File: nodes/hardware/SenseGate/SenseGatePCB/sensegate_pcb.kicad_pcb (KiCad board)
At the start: 2 copper layers, 64.6 x 110 mm, 32 parts, among them J3 Conn_01x02_Socket, J4 Conn_01x24_Pin, J5 Conn_01x04_Socket, J6 Conn_01x04_Socket, J7 Conn_01x04_Socket, J8 Conn_01x04_Socket, J9 Conn_01x04_Socket, Q4 SS8050, SW5 SW_DPDT_x2, U1 DD05CVSA, U2 mt3608_dcdc_converter

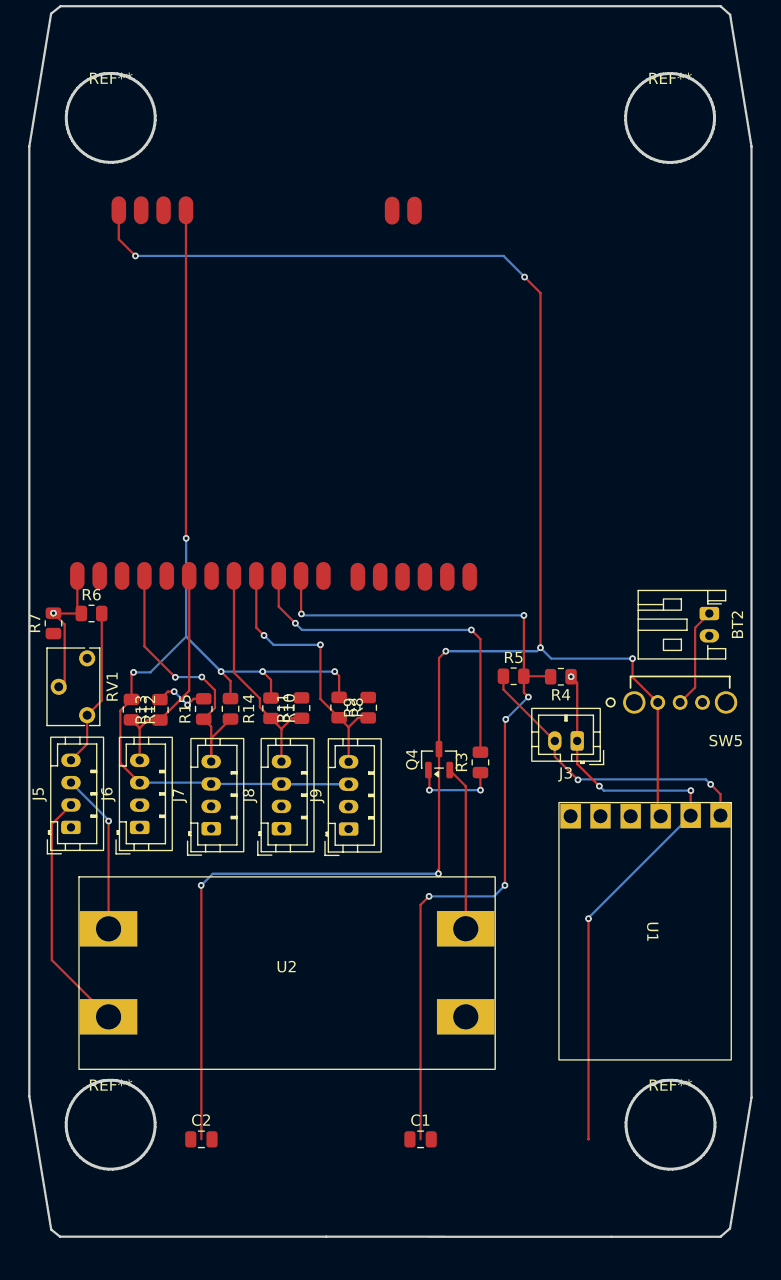
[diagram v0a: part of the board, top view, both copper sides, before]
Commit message: mounting holes for battery added and add schematic for 7.8mm holes
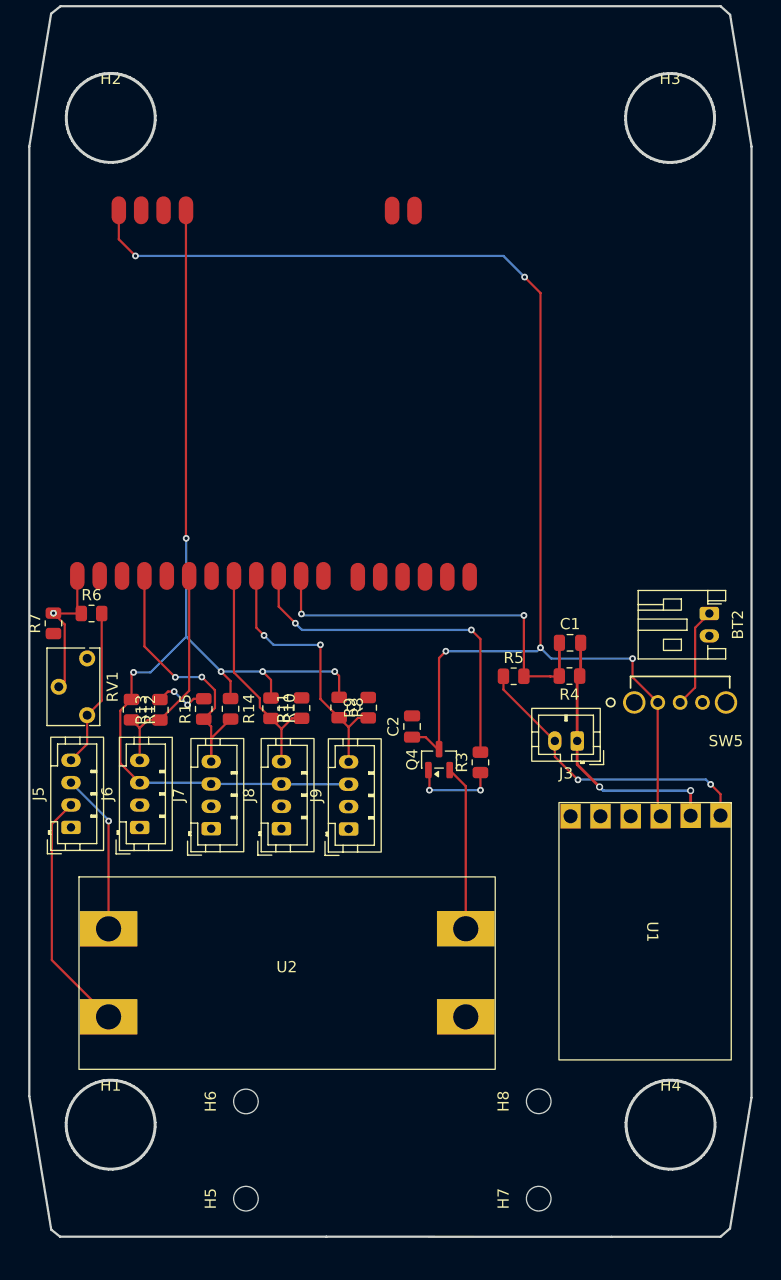
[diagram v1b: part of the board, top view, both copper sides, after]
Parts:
- removed REF** (x4): mounting_hole_7.8mm, SenseGateLib:mounting_hole_7.8mm
- added H1: MountingHole, SenseGateLib:mounting_hole_7.8mm, F.Cu at (102.6, 139.0)
- added H2: MountingHole, SenseGateLib:mounting_hole_7.8mm, F.Cu at (102.6, 49.0)
- added H3: MountingHole, SenseGateLib:mounting_hole_7.8mm, F.Cu at (152.6, 49.0)
- added H4: MountingHole, SenseGateLib:mounting_hole_7.8mm, F.Cu at (152.6, 139.0)
- added H5: MountingHole, MountingHole:MountingHole_2.2mm_M2, F.Cu at (114.7, 145.6)
- added H6: MountingHole, MountingHole:MountingHole_2.2mm_M2, F.Cu at (114.7, 136.9)
- added H7: MountingHole, MountingHole:MountingHole_2.2mm_M2, F.Cu at (140.8, 145.6)
- added H8: MountingHole, MountingHole:MountingHole_2.2mm_M2, F.Cu at (140.8, 136.9)
- moved C1 46.3 mm to (143.7, 95.9)
- moved C2 41.4 mm to (129.5, 103.4), turned to 90 degrees
- moved R4 0.77 mm to (143.6, 98.9)
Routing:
- net VBAT: track 170.8 -> 118.2 mm, vias 7 -> 5
- net MON_SOLAR: track 80.2 -> 35.0 mm, vias 6 -> 2
- net Net-(J3-Pin_1): track 54.1 -> 24.4 mm, vias 4 -> 2
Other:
- board text added: "SenseGate v1 16/06/2026"

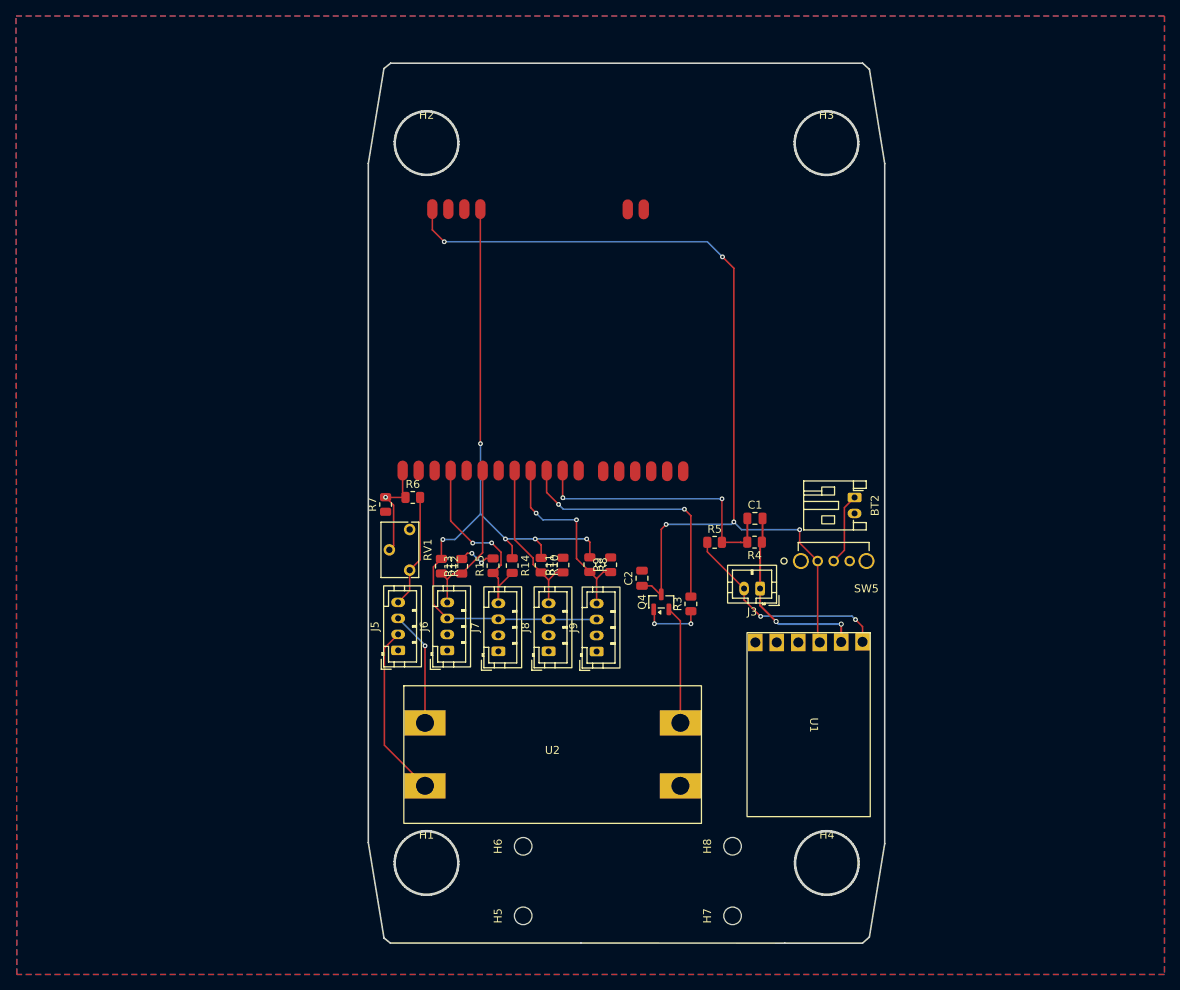
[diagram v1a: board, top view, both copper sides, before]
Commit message: removed most drc errors
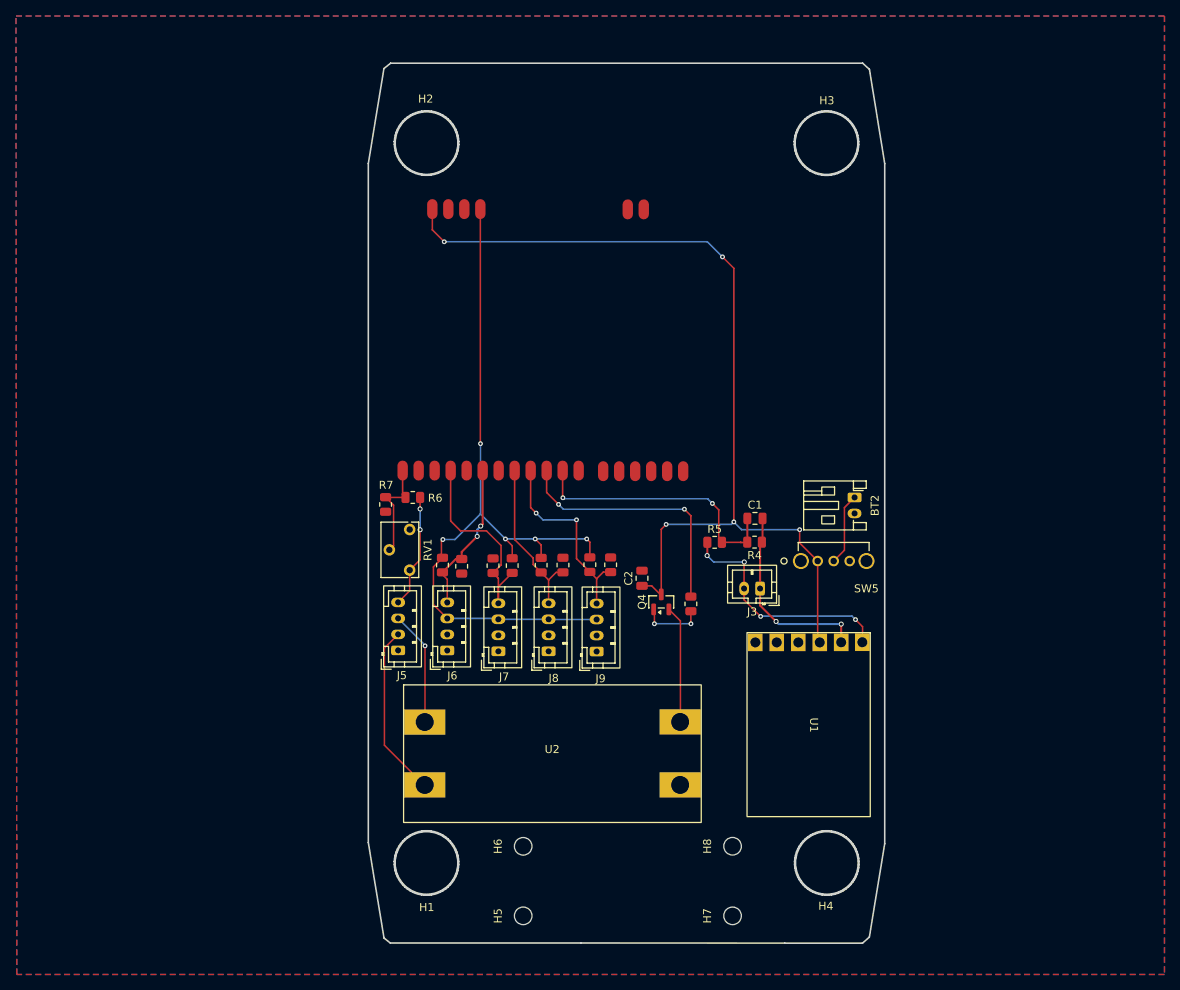
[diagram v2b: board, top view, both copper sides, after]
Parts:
- moved R12 0.20 mm to (104.6, 101.7)
- moved U2 0.11 mm to (118.3, 125.3)
- turned R13 to -90 degrees
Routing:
- net GND: track 4.94 -> 0.00 mm, vias 2 -> 0
- net Net-(J3-Pin_2): track 27.2 -> 29.5 mm, vias 2 -> 4
- net MON_SOLAR: track 35.0 -> 33.9 mm
- net reed_sw_02_measure: track 20.0 -> 19.2 mm, vias 0 -> 2
- net reed_sw_03_measure: track 25.8 -> 26.3 mm, vias 2 -> 0
- net Net-(J5-Pin_4): vias 0 -> 2
- net IS_ADC: vias 1 -> 0

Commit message: fixed EVERYdrc error :)
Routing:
- net Net-(J3-Pin_2): track 29.5 -> 31.5 mm
- net Net-(J3-Pin_1): track 24.4 -> 24.9 mm
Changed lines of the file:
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@@
-	)
-	(segment
-		(start 155.78 108.1)
-		(end 144.4 108.1)
-		(width 0.2)
-		(layer "B.Cu")
-		(net "Net-(J3-Pin_2)")
 	)
 	(segment
 		(start 156.22 108.54)
-		(end 155.78 108.1)
+		(end 153.4 105.72)
 		(width 0.2)
 		(layer "B.Cu")
@@
 		(start 142.31 101.34)
 		(end 138.49 101.34)
+		(width 0.2)
+		(layer "B.Cu")
+		(net "Net-(J3-Pin_2)")
+	)
+	(segment
+		(start 146.78 105.72)
+		(end 144.36 108.14)
 		(width 0.2)
 		(layer "B.Cu")
@@
 	)
 	(segment
-		(start 144.4 108.1)
-		(end 144.36 108.14)
+		(start 153.4 105.72)
+		(end 146.78 105.72)
 		(width 0.2)
 		(layer "B.Cu")
@@
 	)
 	(segment
-		(start 146.29 108.77)
-		(end 144.29 106.77)
-		(width 0.254)
-		(layer "F.Cu")
-		(net "Net-(J3-Pin_1)")
-	)
-	(segment
-		(start 154.43 111.34)
-		(end 154.43 109.1)
+		(start 154.44 109.11)
+		(end 154.44 111.33)
 		(width 0.254)
 		(layer "F.Cu")
@@
 	)
 	(segment
-		(start 144.29 106.77)
-		(end 144.29 104.66)
+		(start 145.09 107.57)
+		(end 144.29 106.77)
+		(width 0.254)
+		(layer "F.Cu")
+		(net "Net-(J3-Pin_1)")
+	)
+	(segment
+		(start 146.25 107.57)
+		(end 145.09 107.57)
+		(width 0.254)
+		(layer "F.Cu")
+		(net "Net-(J3-Pin_1)")
+	)
+	(segment
+		(start 154.44 111.33)
+		(end 154.43 111.34)
 		(width 0.254)
 		(layer "F.Cu")
@@
 	)
 	(segment
+		(start 144.29 106.77)
+		(end 144.29 104.66)
+		(width 0.254)
+		(layer "F.Cu")
+		(net "Net-(J3-Pin_1)")
+	)
+	(segment
+		(start 153.5 108.17)
+		(end 154.44 109.11)
+		(width 0.254)
+		(layer "F.Cu")
+		(net "Net-(J3-Pin_1)")
+	)
+	(segment
 		(start 144.29 99.265)
 		(end 144.29 104.66)
@@
 	)
 	(via
-		(at 154.43 109.1)
+		(at 153.5 108.17)
 		(size 0.635)
 		(drill 0.381)
@@
 	)
 	(via
-		(at 146.29 108.77)
+		(at 146.25 107.57)
 		(size 0.635)
 		(drill 0.381)
@@
 	)
 	(segment
-		(start 154.43 109.1)
-		(end 146.62 109.1)
+		(start 148.13 106.93)
+		(end 147.49 107.57)
 		(width 0.254)
 		(layer "B.Cu")
@@
 	)
 	(segment
-		(start 146.62 109.1)
-		(end 146.29 108.77)
+		(start 147.49 107.57)
+		(end 146.25 107.57)
 		(width 0.254)
 		(layer "B.Cu")
+		(net "Net-(J3-Pin_1)")
+	)
+	(segment
+		(start 152.26 106.93)
+		(end 148.13 106.93)
+		(width 0.254)
+		(layer "B.Cu")
+		(net "Net-(J3-Pin_1)")
+	)
+	(segment
+		(start 153.5 108.17)
+		(end 152.26 106.93)
+		(width 0.254)
+		(layer "B.Cu")

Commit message: gerber files created
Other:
- board text added: "sensemate goes here"

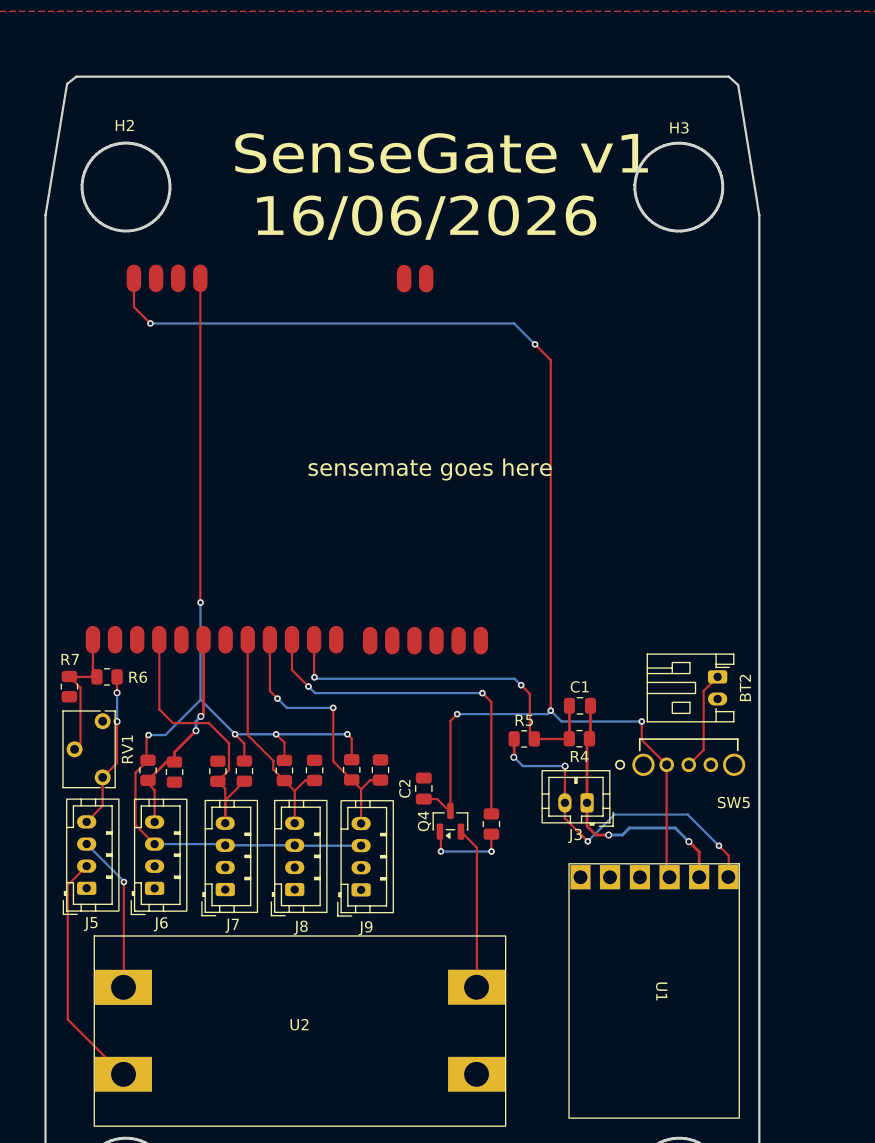
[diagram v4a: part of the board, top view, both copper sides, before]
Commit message: implemented michels complaints, todo: rulechecker and gen gerber files
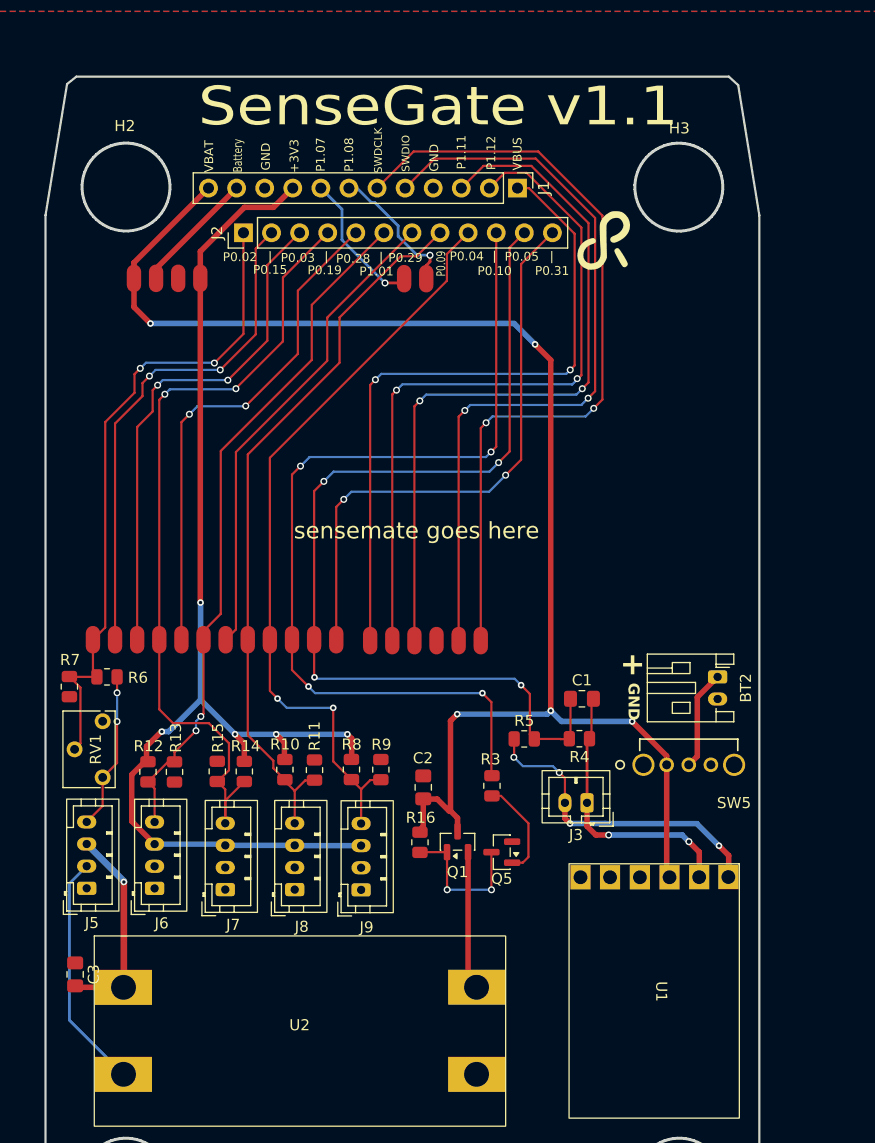
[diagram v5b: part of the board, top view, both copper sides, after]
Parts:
- removed Q4: SS8050, Package_TO_SOT_SMD:SOT-23
- added C3: C, Capacitor_SMD:C_0805_2012Metric_Pad1.18x1.45mm_HandSolder, F.Cu at (98.0, 120.2)
- added G***: LOGO, LOGO, F.Cu at (148.4, 53.8)
- added J1: Conn_01x12_Pin, Connector_PinHeader_2.54mm:PinHeader_1x12_P2.54mm_Vertical, F.Cu at (138.0, 49.1)
- added J2: Conn_01x12_Pin, Connector_PinHeader_2.54mm:PinHeader_1x12_P2.54mm_Vertical, F.Cu at (113.2, 53.1)
- added Q1: AO3401A, Package_TO_SOT_SMD:SOT-23, F.Cu at (132.6, 108.2)
- added Q5: SS8050, Package_TO_SOT_SMD:SOT-23, F.Cu at (136.6, 109.1)
- added R16: R, Resistor_SMD:R_0805_2012Metric, F.Cu at (129.2, 108.2)
- C1, C2: footprint Capacitor_SMD:C_0805_2012Metric -> Capacitor_SMD:C_0805_2012Metric_Pad1.18x1.45mm_HandSolder
- moved R3 3.46 mm to (135.7, 103.1)
- moved C1 0.66 mm to (143.8, 95.2)
- moved R12 0.14 mm to (104.6, 101.9)
- moved C2 0.12 mm to (129.5, 103.3)
- moved R10 0.09 mm to (117.0, 101.7)
- moved R15 0.06 mm to (110.9, 101.8)
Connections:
- J4 pad Battery: unconnected-(J4-Pin_23-PadBattery) -> Net-(J1-Pin_11)
- J4 pad P0.03_A1_D1_/_lora_rst: unconnected-(J4-Pin_3-PadP0.03_A1_D1_/_lora_rst) -> Net-(J2-Pin_3)
- J4 pad P0.15_D11_/_lora_dio0: unconnected-(J4-Pin_2-PadP0.15_D11_/_lora_dio0) -> Net-(J2-Pin_2)
- J4 pad P0.28_A2_D2_/_lora_dio1: unconnected-(J4-Pin_5-PadP0.28_A2_D2_/_lora_dio1) -> Net-(J2-Pin_5)
- J4 pad P0.29_A3_D3_/_lora_dio2: unconnected-(J4-Pin_7-PadP0.29_A3_D3_/_lora_dio2) -> Net-(J2-Pin_7)
- J4 pad P0.31_D16: unconnected-(J4-Pin_12-PadP0.31_D16) -> Net-(J2-Pin_12)
- J4 pad P1.05_D18_/_spi_miso1: unconnected-(J4-Pin_19-PadP1.05_D18_/_spi_miso1) -> Net-(J1-Pin_7)
- J4 pad P1.07_D19_/_spi_mosi1: unconnected-(J4-Pin_20-PadP1.07_D19_/_spi_mosi1) -> Net-(J1-Pin_8)
- J4 pad P1.11_D6_/_pogo_tx: unconnected-(J4-Pin_15-PadP1.11_D6_/_pogo_tx) -> Net-(J1-Pin_3)
- J4 pad P1.12_D7_/_pogo_rx: unconnected-(J4-Pin_14-PadP1.12_D7_/_pogo_rx) -> Net-(J1-Pin_2)
- J4 pad SWDCLK_/_pogo_swdclk: unconnected-(J4-Pin_18-PadSWDCLK_/_pogo_swdclk) -> Net-(J1-Pin_6)
- J4 pad SWDIO_/_pogo_swdio: unconnected-(J4-Pin_17-PadSWDIO_/_pogo_swdio) -> Net-(J1-Pin_5)
- J4 pad VBUS_/_pogo_vbus: unconnected-(J4-Pin_13-PadVBUS_/_pogo_vbus) -> Net-(J1-Pin_1)
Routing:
- net Net-(J1-Pin_6): track 0.00 -> 72.1 mm, vias 0 -> 2
- net Net-(J1-Pin_5): track 0.00 -> 69.7 mm, vias 0 -> 2
- net Net-(J1-Pin_3): track 0.00 -> 66.7 mm, vias 0 -> 2
- net Net-(J1-Pin_2): track 0.00 -> 64.4 mm, vias 0 -> 2
- net Net-(J1-Pin_1): track 0.00 -> 61.1 mm, vias 0 -> 2
- net MON_SOLAR: track 33.9 -> 87.5 mm, vias 2 -> 4
- net Net-(J2-Pin_12): track 0.00 -> 52.2 mm, vias 0 -> 2
- net TOG_20V: track 32.1 -> 82.4 mm, vias 2 -> 4
- net reed_sw_03_measure: track 26.3 -> 72.9 mm, vias 0 -> 2
- net Net-(J2-Pin_3): track 0.00 -> 46.3 mm, vias 0 -> 2
- net IS_ADC: track 13.2 -> 59.3 mm, vias 0 -> 2
- net Net-(J2-Pin_2): track 0.00 -> 46.1 mm, vias 0 -> 2
- net Net-(J2-Pin_5): track 0.00 -> 45.9 mm, vias 0 -> 2
- net reed_sw_01_measure: track 20.5 -> 65.4 mm
- net reed_sw_04_measure: track 24.6 -> 68.8 mm
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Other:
- board text added: "+"
- board text added: "+3V3"
- board text added: "Battery"
- board text added: "GND"
- board text added: "P0.02"
- board text added: "P0.03"
- board text added: "P0.04"
- board text added: "P0.05"
- board text added: "P0.09"
- board text added: "P0.10"
- board text added: "P0.15"
- board text added: "P0.19"
- board text added: "P0.28"
- board text added: "P0.29"
- board text added: "P0.31"
- board text added: "P1.01"
- board text added: "P1.07"
- board text added: "P1.08"
- board text added: "P1.11"
- board text added: "P1.12"
- board text added: "R3"
- board text added: "SWDCLK"
- board text added: "SWDIO"
- board text added: "SenseGate v1.1"
- board text added: "VBAT"
- board text added: "VBUS"
- board text added: "|"
- board text removed: "SenseGate v1 16/06/2026"
